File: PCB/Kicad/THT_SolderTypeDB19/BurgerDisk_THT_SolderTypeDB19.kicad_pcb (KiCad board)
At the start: 2 copper layers, 93.7 x 67.6 mm, 18 parts, among them J1 Daisy port in, J2 MicroSD module, J3 UART, J4 Daisy port out, U1 PC817

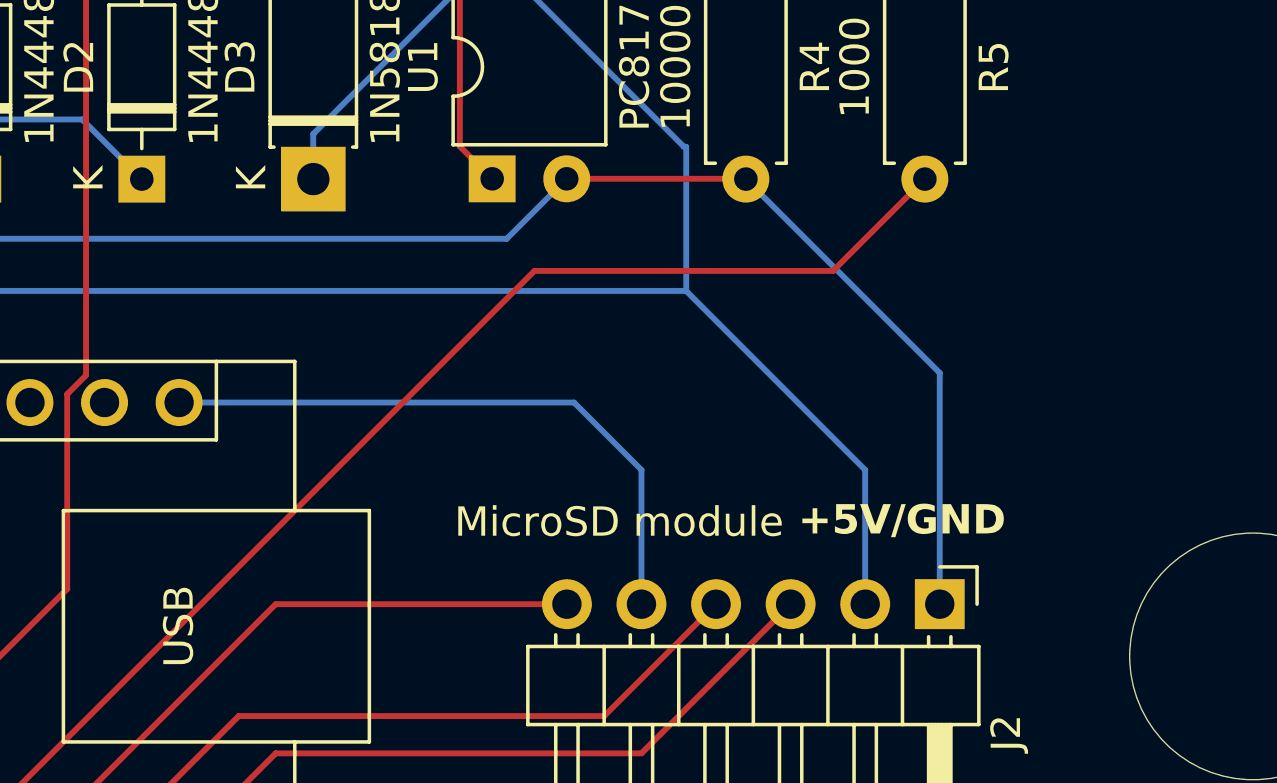
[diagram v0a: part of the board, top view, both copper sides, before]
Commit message: Add 8-pin header for full size SD module
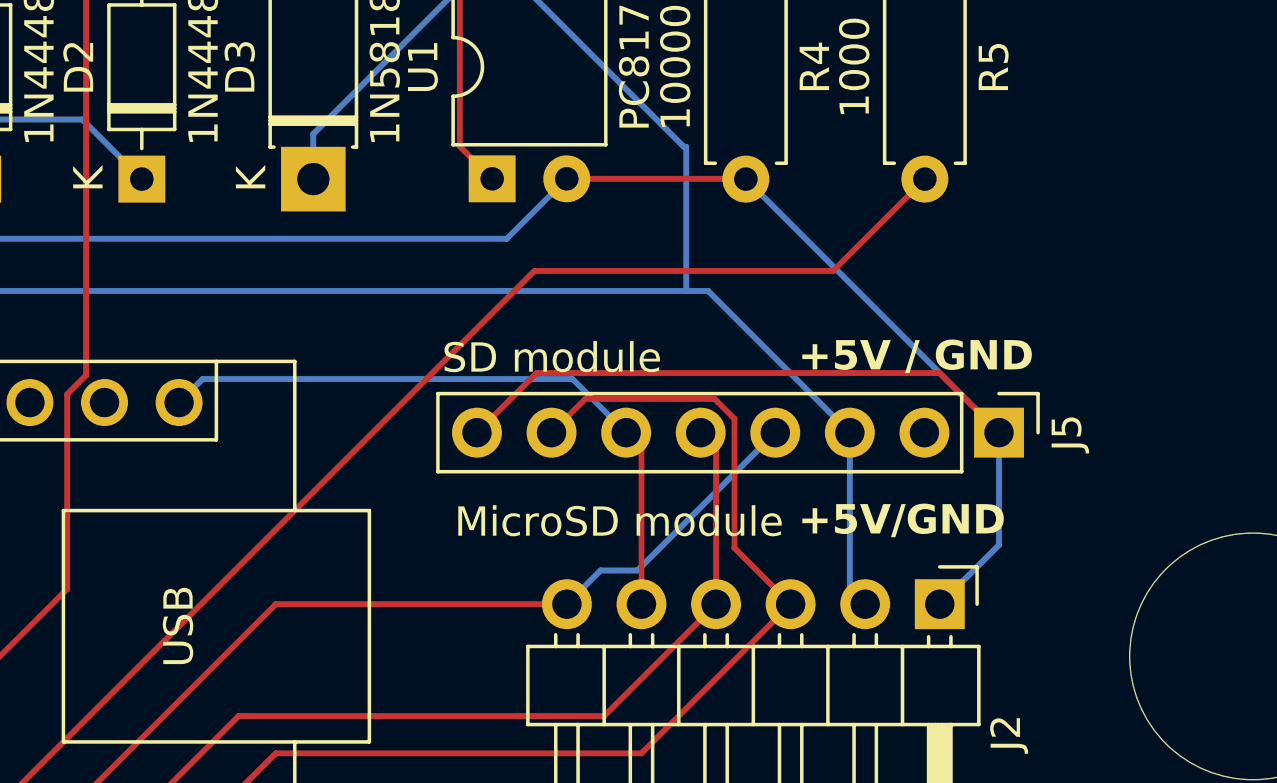
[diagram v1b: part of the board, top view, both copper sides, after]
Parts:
- added J5: SD module, Connector_PinHeader_2.54mm:PinHeader_1x08_P2.54mm_Vertical, F.Cu at (148.3, 93.7)
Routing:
- net GND: track 179.7 -> 200.9 mm
- net MISO: track 24.3 -> 38.4 mm
- net CS: track 21.8 -> 31.3 mm
- net MOSI: track 24.3 -> 30.4 mm
- net SCK: track 21.3 -> 22.4 mm
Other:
- board text added: "+5V / GND"

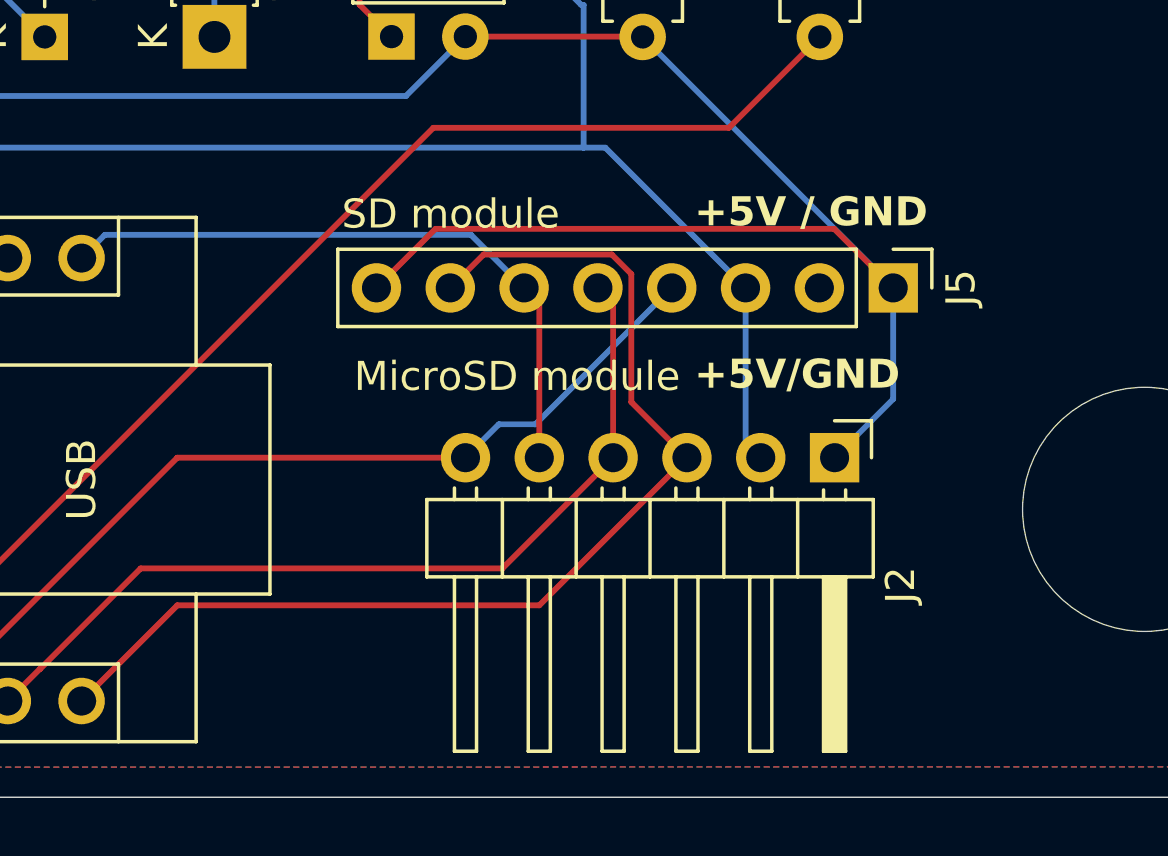
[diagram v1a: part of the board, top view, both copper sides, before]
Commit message: Vertical footprints
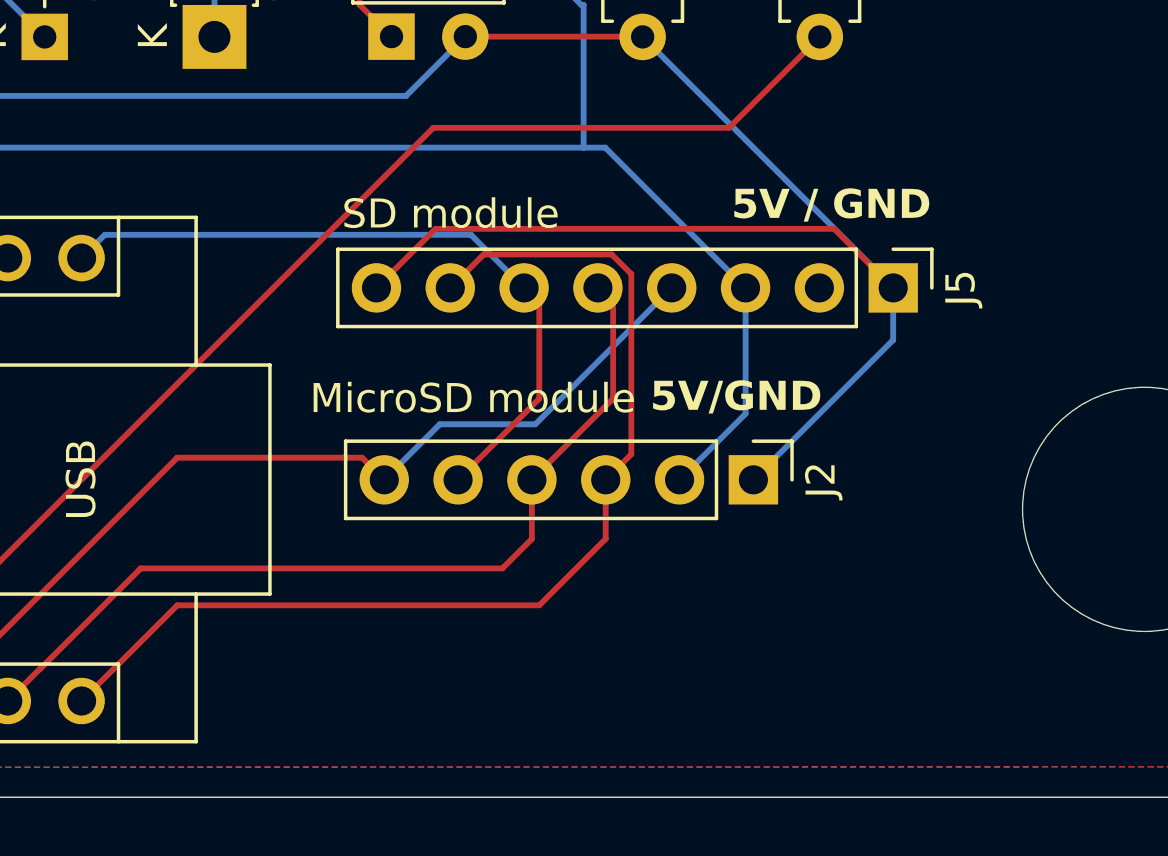
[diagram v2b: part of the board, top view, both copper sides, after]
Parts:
- J2: footprint Connector_PinHeader_2.54mm:PinHeader_1x06_P2.54mm_Horizontal -> Connector_PinHeader_2.54mm:PinHeader_1x06_P2.54mm_Vertical
- moved J2 2.90 mm to (143.5, 100.3)
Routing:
- net GND: track 200.9 -> 202.8 mm
- net SCK: track 22.4 -> 24.3 mm
- net MISO: track 38.4 -> 36.8 mm
- net 5V_burgerDisk: track 86.0 -> 87.5 mm
- net CS: track 31.3 -> 31.9 mm
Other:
- board text added: "5V / GND"
- board text added: "5V/GND"
- board text removed: "+5V / GND"
- board text removed: "+5V/GND"

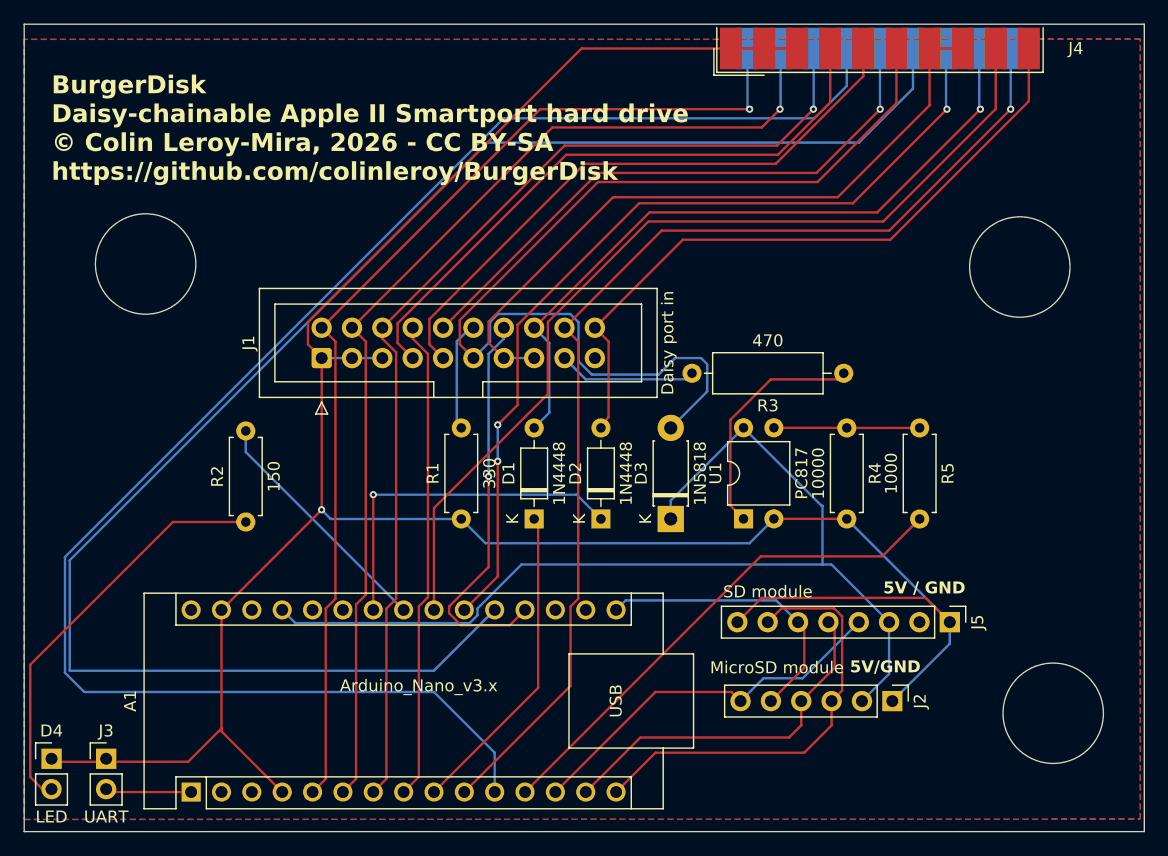
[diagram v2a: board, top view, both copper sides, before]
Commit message: Revert full-size SD connector and module.
They don't have level shifter.
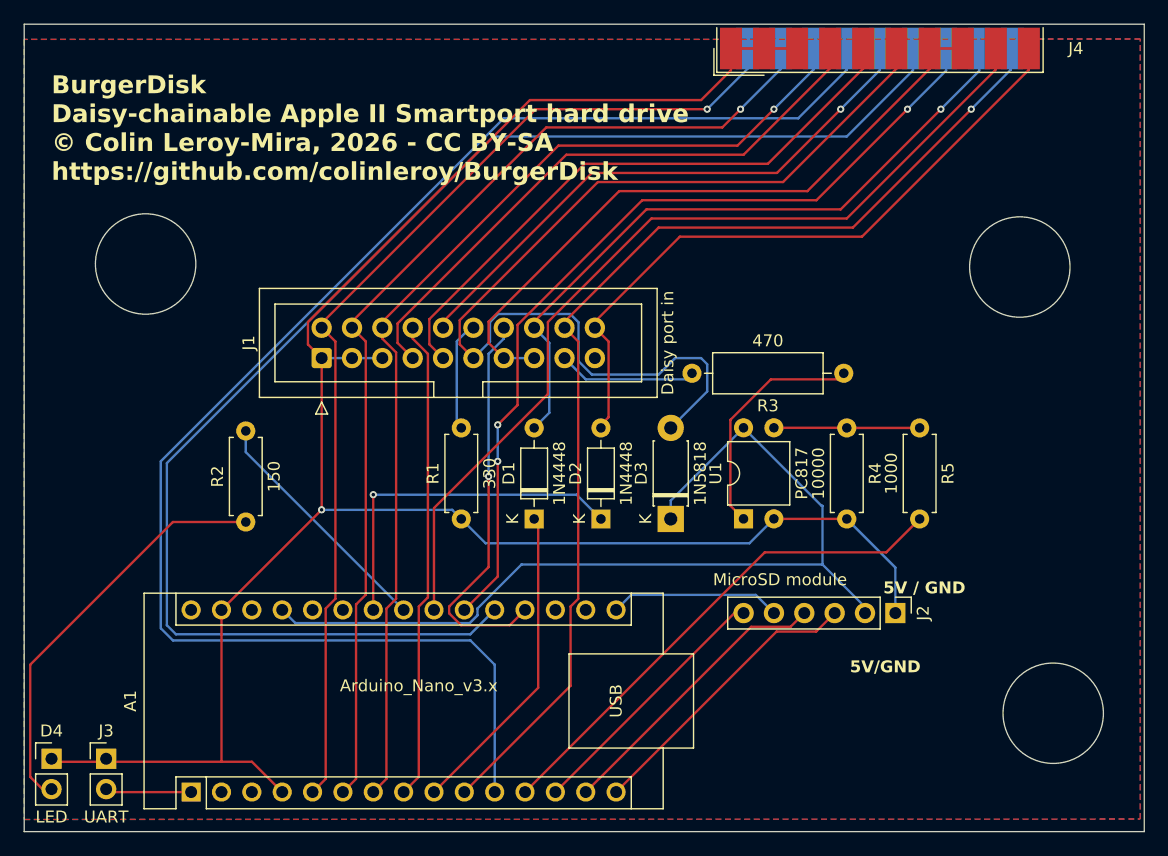
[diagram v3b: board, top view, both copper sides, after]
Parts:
- removed J5: SD module, Connector_PinHeader_2.54mm:PinHeader_1x08_P2.54mm_Vertical
- moved J2 7.37 mm to (143.8, 93.0)
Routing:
- net GND: track 202.8 -> 173.5 mm
- net HDSEL_out: track 137.2 -> 120.0 mm
- net MISO: track 36.8 -> 24.5 mm
- net PH3_out: track 136.6 -> 126.6 mm
- net CS: track 31.9 -> 22.0 mm
- net SCK: track 24.3 -> 14.4 mm
- net 5V_burgerDisk: track 87.5 -> 77.9 mm
- net MOSI: track 30.4 -> 24.5 mm
- net PH0: track 88.7 -> 86.7 mm
- net DRV1_out: track 74.2 -> 72.2 mm
- net DRV2_out: track 78.0 -> 76.0 mm
- net +12V: track 58.0 -> 56.3 mm
- net RDDATA_out: track 59.5 -> 57.8 mm
- net EN3.5: track 51.8 -> 50.1 mm
- net 5V_apple2: track 85.7 -> 84.0 mm
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
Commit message: Align connectors
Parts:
- moved J2 14.7 mm to (143.8, 107.7)
- moved J4 1.50 mm to (141.0, 45.7)
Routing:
- net SCK: track 14.4 -> 29.2 mm
- net 5V_burgerDisk: track 77.9 -> 92.7 mm
- net GND: track 173.5 -> 187.6 mm
- net CS: track 22.0 -> 16.9 mm
- net MISO: track 24.5 -> 20.1 mm
- net MOSI: track 24.5 -> 21.5 mm
- net +12V: track 56.3 -> 55.6 mm
- net HDSEL_out: track 120.0 -> 119.4 mm
- net WRDATA: track 91.7 -> 91.1 mm
- net PH3_out: track 126.6 -> 126.0 mm
- net PH0: track 86.7 -> 86.0 mm
- net DRV2_out: track 76.0 -> 75.4 mm
- net WRPROT_out: track 56.6 -> 55.9 mm
- net WREQ: track 47.6 -> 47.0 mm
- net RDDATA_out: track 57.8 -> 57.1 mm
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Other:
- board text removed: "5V / GND"
